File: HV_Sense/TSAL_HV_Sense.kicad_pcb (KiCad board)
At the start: 2 copper layers, 100 x 50 mm, 34 parts, among them J1 Nano-Fit, J2 Mini-SPOX, J3 Nano-Fit, J4 Mini-SPOX, J5 Mini-SPOX, J6 Mini-SPOX, U1 4N35, U2 4N35

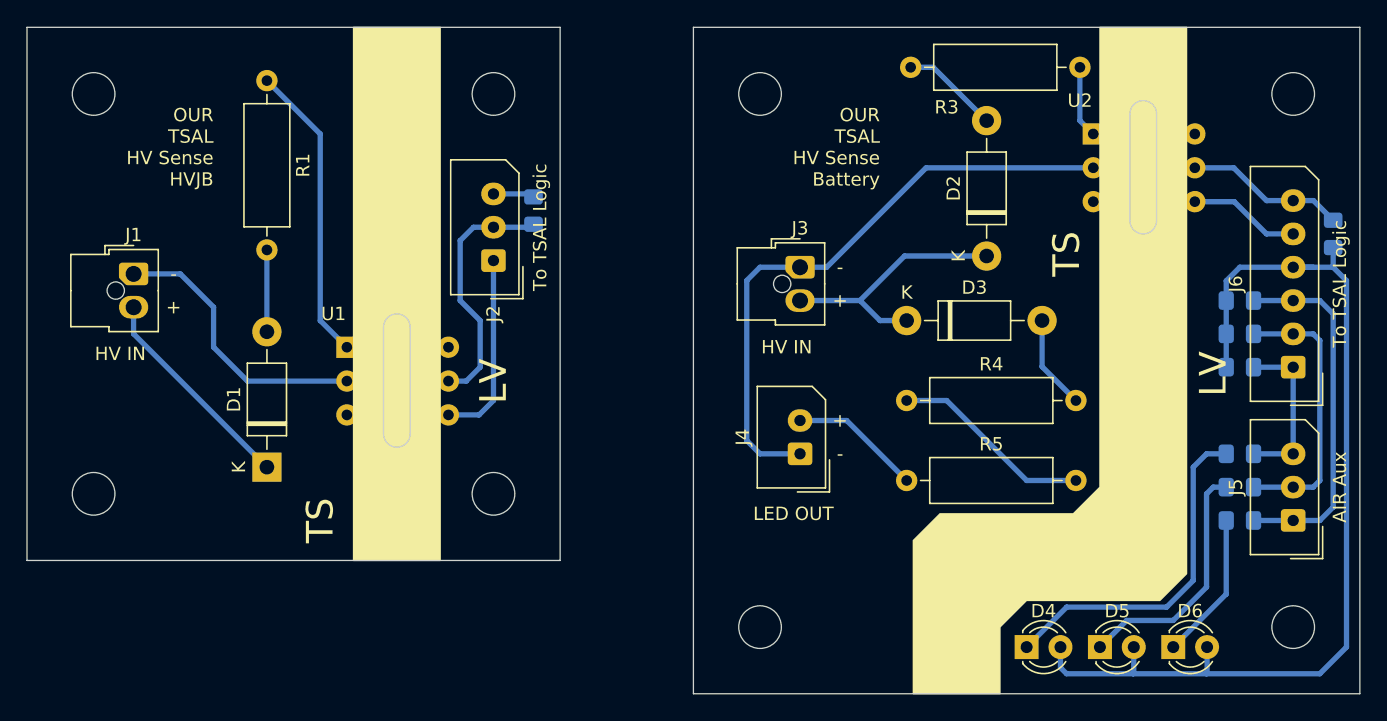
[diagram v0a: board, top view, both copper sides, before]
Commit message: HV_Sense: change hv input connector to Micro-Fit
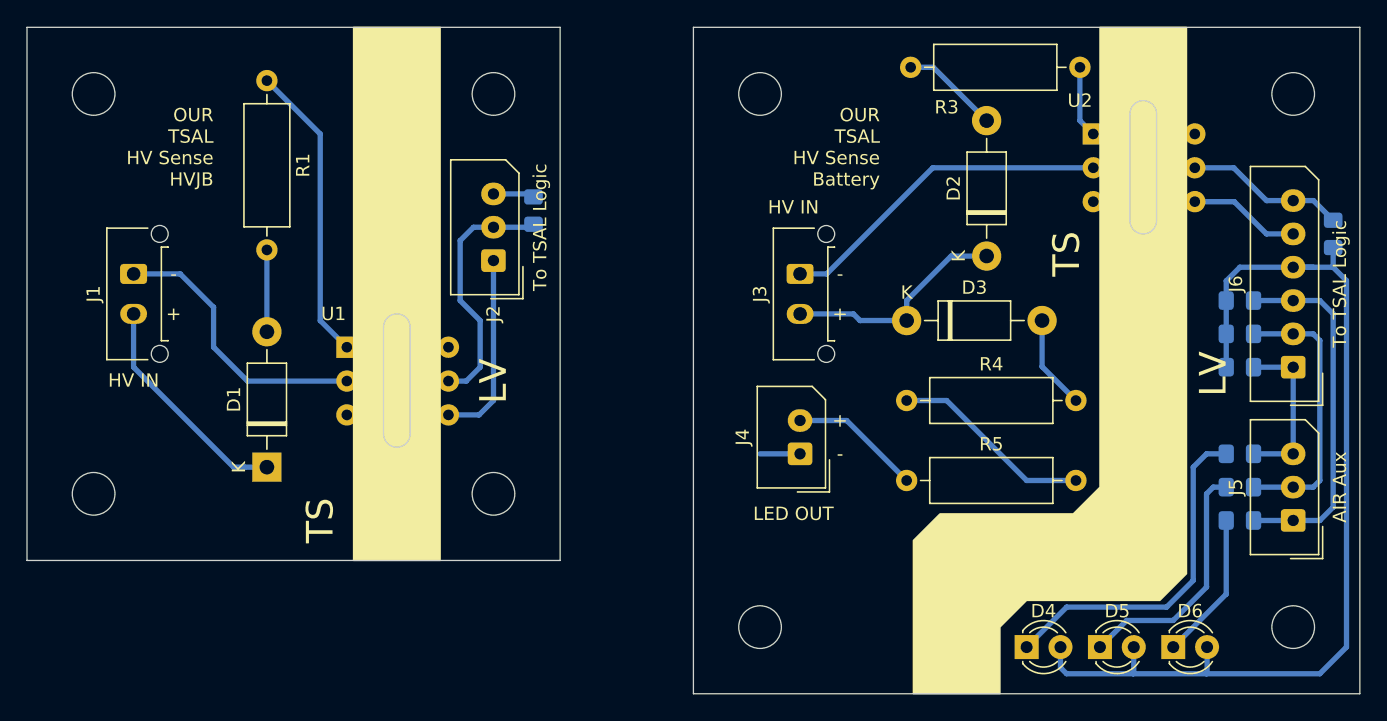
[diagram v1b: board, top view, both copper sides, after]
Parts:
- J1, J3: value Nano-Fit -> Micro-Fit; footprint Connector_Molex:Molex_Nano-Fit_105309-xx02_1x02_P2.50mm_Vertical -> Connector_Molex:Molex_Micro-Fit_3.0_43650-0215_1x02_P3.00mm_Vertical
- moved J3 0.51 mm to (98.0, 58.5), turned to 270 degrees
- turned J1 to 270 degrees
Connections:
- U1 pad 3: (no net) -> Net-(U1-Pad3)
- U1 pad 6: (no net) -> Net-(U1-Pad6)
- U2 pad 3: (no net) -> Net-(U2-Pad3)
- U2 pad 6: (no net) -> Net-(U2-Pad6)
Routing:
- net /HV-: track 67.0 -> 49.4 mm
- net /HV+: track 35.6 -> 34.2 mm

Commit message: HV_Sense: update schematics
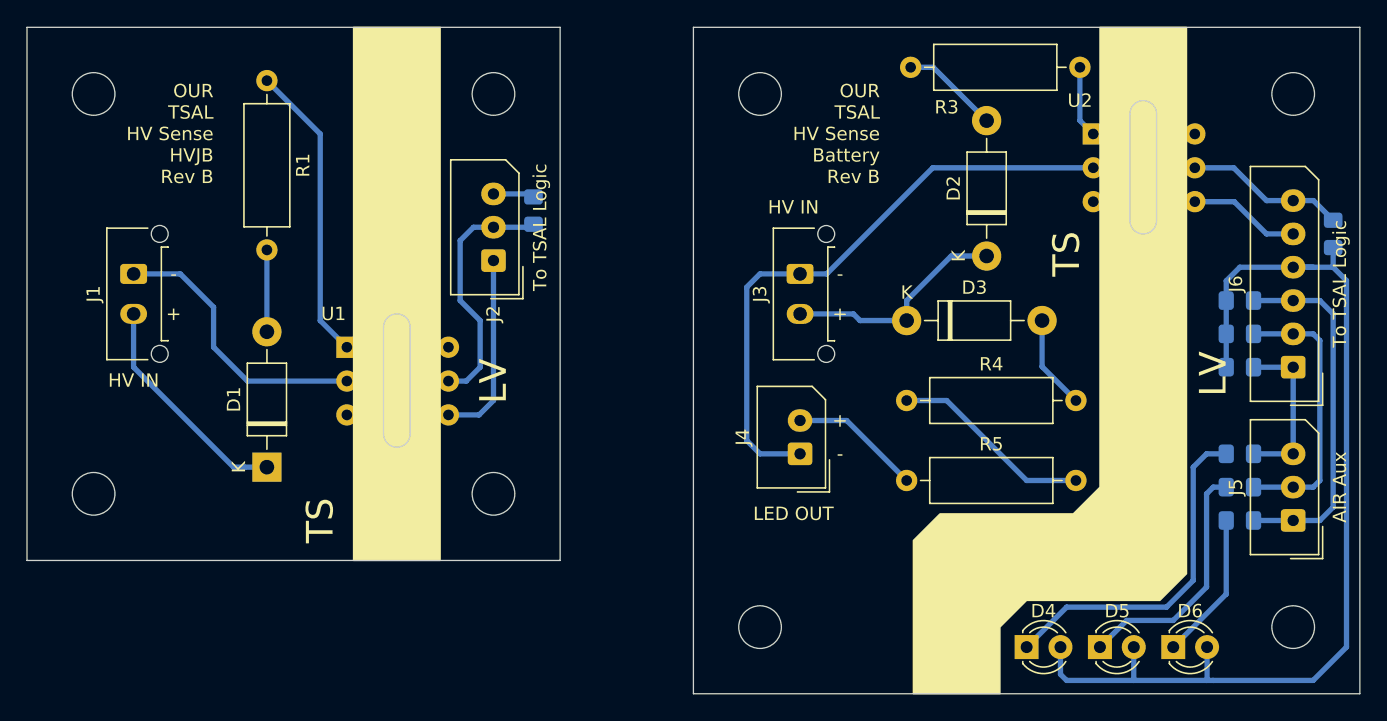
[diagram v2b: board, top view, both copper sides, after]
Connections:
- net /AUX_1 renamed Net-(J5-Pad1)
- net /AUX_2 renamed Net-(J5-Pad2)
- net /AUX_3 renamed Net-(J5-Pad3)
- D1 pad 1: /HV+ -> Net-(D1-Pad1)
- D2 pad 1: /HV+ -> Net-(D2-Pad1)
- D3 pad 1: /HV+ -> Net-(D2-Pad1)
- D4 pad 2: /VCC -> Net-(D4-Pad2)
- D5 pad 2: /VCC -> Net-(D4-Pad2)
- D6 pad 2: /VCC -> Net-(D4-Pad2)
- J1 pad 1: /HV- -> Net-(J1-Pad1)
- J1 pad 2: /HV+ -> Net-(D1-Pad1)
- J2 pad 1: /GND -> Net-(J2-Pad1)
- J2 pad 2: /Sense -> Net-(J2-Pad2)
- J2 pad 3: /VCC -> Net-(J2-Pad3)
- J3 pad 1: /HV- -> Net-(J3-Pad1)
- J3 pad 2: /HV+ -> Net-(D2-Pad1)
- J4 pad 1: /HV- -> Net-(J3-Pad1)
- J6 pad 4: /VCC -> Net-(D4-Pad2)
- J6 pad 5: /GND -> Net-(J6-Pad5)
- J6 pad 6: /Sense -> Net-(J6-Pad6)
- R2 pad 1: /VCC -> Net-(J2-Pad3)
- R2 pad 2: /Sense -> Net-(J2-Pad2)
- R6 pad 1: /Sense -> Net-(J6-Pad6)
- R6 pad 2: /VCC -> Net-(D4-Pad2)
- R7 pad 1: /VCC -> Net-(D4-Pad2)
- R8 pad 1: /VCC -> Net-(D4-Pad2)
- R9 pad 1: /VCC -> Net-(D4-Pad2)
- U1 pad 2: /HV- -> Net-(J1-Pad1)
- U1 pad 4: /GND -> Net-(J2-Pad1)
- U1 pad 5: /Sense -> Net-(J2-Pad2)
- U2 pad 2: /HV- -> Net-(J3-Pad1)
- U2 pad 4: /GND -> Net-(J6-Pad5)
- U2 pad 5: /Sense -> Net-(J6-Pad6)
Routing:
- net /VCC: track 78.0 -> 0.00 mm
- net Net-(D4-Pad2): track 0.00 -> 76.6 mm
- net /HV-: track 49.4 -> 0.00 mm
- net Net-(J3-Pad1): track 0.00 -> 45.6 mm
- net /HV+: track 34.2 -> 0.00 mm
- net /Sense: track 31.0 -> 0.00 mm
- net /GND: track 22.7 -> 0.00 mm
- net Net-(J1-Pad1): track 0.00 -> 21.1 mm
- net Net-(J2-Pad2): track 0.00 -> 19.0 mm
- net Net-(D1-Pad1): track 0.00 -> 17.1 mm
- net Net-(D2-Pad1): track 0.00 -> 17.1 mm
- net Net-(J2-Pad1): track 0.00 -> 14.3 mm
- net Net-(J6-Pad6): track 0.00 -> 12.0 mm
- net Net-(J6-Pad5): track 0.00 -> 8.38 mm
- net Net-(J2-Pad3): track 0.00 -> 3.09 mm
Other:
- board text added: "OUR TSAL HV Sense Battery Rev B"
- board text added: "OUR TSAL HV Sense HVJB Rev B"
- board text removed: "OUR TSAL HV Sense Battery"
- board text removed: "OUR TSAL HV Sense HVJB"
